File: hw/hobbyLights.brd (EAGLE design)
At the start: 50 x 35 mm, 56 parts, among them U1 MCP73831-2, U2 POWER, U3 BD48K28G, U4 ATMEGA32U4-AU, U5 TPS61222, Y1 RESONATORSMD

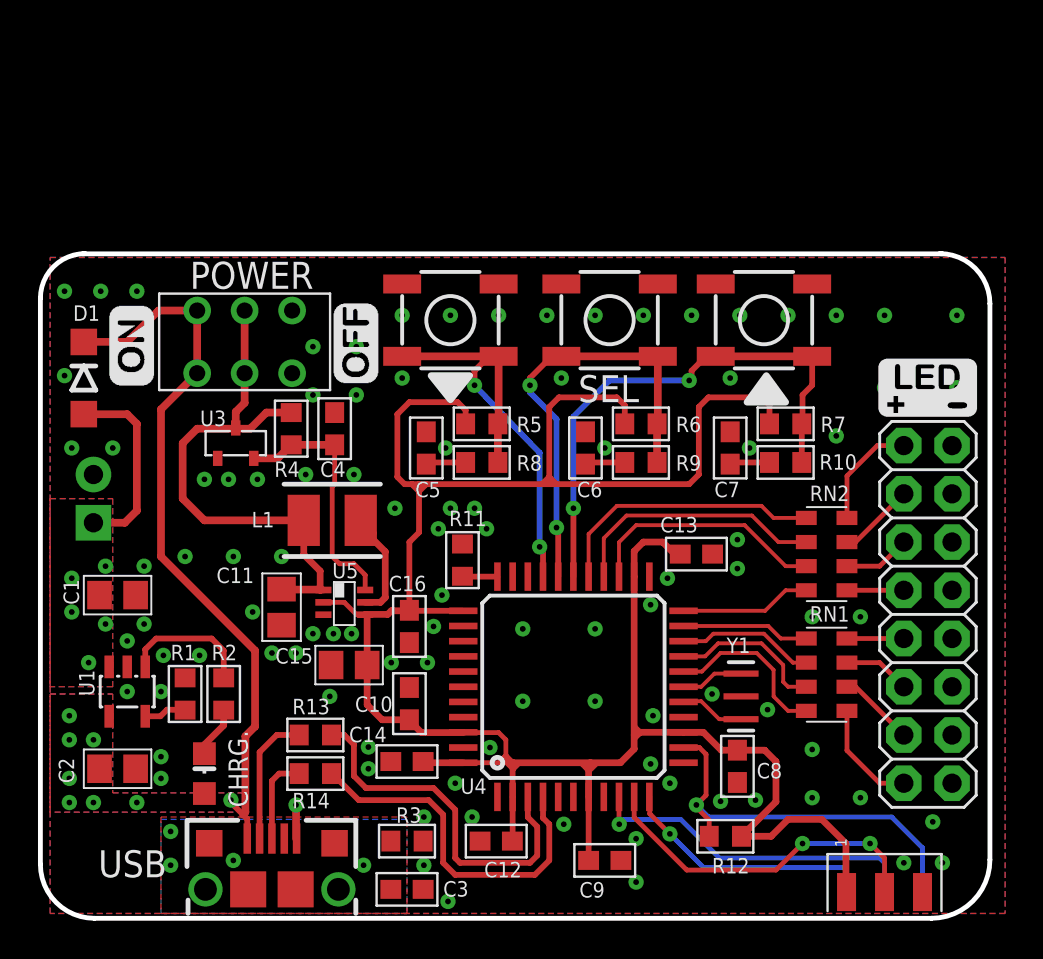
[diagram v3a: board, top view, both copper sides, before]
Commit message: Updated schematic for Rev B.
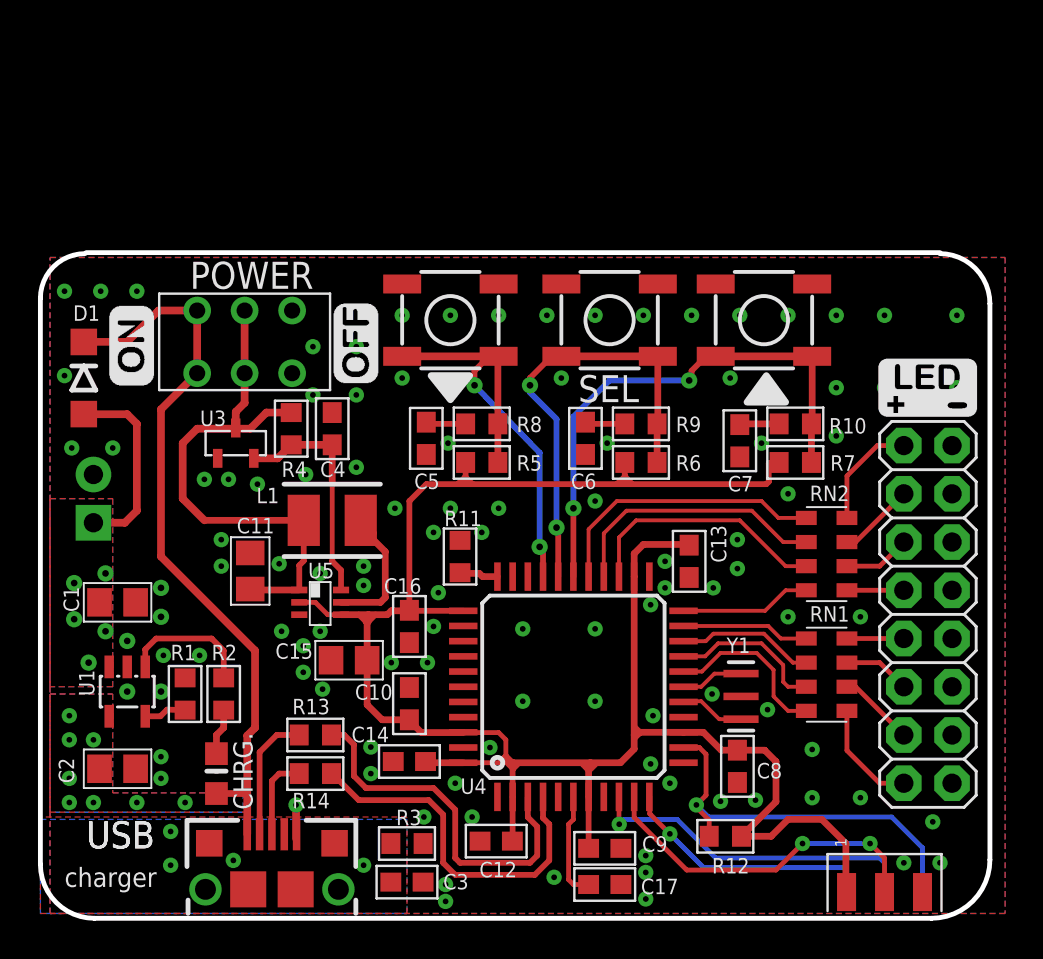
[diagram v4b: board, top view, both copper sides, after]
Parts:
- added C17: 1uF, rcl:C0603
- C5, C6, C7: value 0.1uF -> 0.1nF
- moved C11 2.52 mm to (11.0, 18.3), turned to 90 degrees
- moved R10 2.09 mm to (39.8, 26.0)
- moved R7 2.09 mm to (39.8, 24.0)
- moved R5 2.03 mm to (23.2, 24.0)
- moved R6 2.03 mm to (31.6, 24.0)
- moved R8 2.03 mm to (23.2, 26.0)
- moved R9 2.03 mm to (31.6, 26.0)
- moved U5 1.27 mm to (14.7, 16.6)
- moved CHARGE 0.64 mm to (9.27, 7.62)
- moved C9 0.63 mm to (29.7, 3.68)
- moved C7 0.63 mm to (36.8, 25.1), turned to 270 degrees
- moved C13 0.54 mm to (34.2, 18.8), turned to 270 degrees
- moved C5 0.51 mm to (20.3, 25.3), turned to 270 degrees
- moved C6 0.51 mm to (28.7, 25.3), turned to 270 degrees
- moved C1 0.38 mm to (4.06, 16.6)
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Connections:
- net 3.3V: now also C17.1
- net GND: now also C17.2
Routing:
- net VCC: track 132.7 -> 114.7 mm
- net 3.3V: track 0.00 -> 5.63 mm
- net V_BATT: track 30.9 -> 28.9 mm
- net N$15: track 5.76 -> 7.03 mm
- net PWR_OK: track 13.4 -> 12.3 mm
- net V_USB: track 38.4 -> 38.9 mm
- net GND: track 1.80 -> 2.00 mm, vias 99 -> 106
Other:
- board size 50 x 35 mm -> 50 x 35.1 mm
- board text added: "charger"

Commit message: Updates for production - Rev B
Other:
- board text added: "B"
- board text added: "ICSP"
- board text removed: "A"
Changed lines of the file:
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@@
 <setting verticaltext="up"/>
 </settings>
-<grid distance="0.05" unitdist="inch" unit="mm" style="lines" multiple="1" display="yes" altdistance="5" altunitdist="mil" altunit="mil"/>
+<grid distance="0.05" unitdist="inch" unit="mm" style="lines" multiple="1" display="yes" altdistance="5" altunitdist="mil" altunit="mm"/>
 <layers>
 <layer number="1" name="Top" color="4" fill="1" visible="yes" active="yes"/>
-<layer number="16" name="Bottom" color="1" fill="1" visible="yes" active="yes"/>
+<layer number="16" name="Bottom" color="1" fill="1" visible="no" active="yes"/>
 <layer number="17" name="Pads" color="2" fill="1" visible="yes" active="yes"/>
 <layer number="18" name="Vias" color="2" fill="1" visible="yes" active="yes"/>
@@
 <text x="7.747" y="19.812" size="1.778" layer="22" font="vector" ratio="15" rot="MR0">+</text>
 <text x="33.655" y="15.24" size="1.4224" layer="22" font="vector" ratio="12" rot="MR0">hobby lights</text>
-<text x="33.02" y="11.43" size="1.4224" layer="22" font="vector" ratio="12" rot="MR0">A</text>
+<text x="33.02" y="11.811" size="1.4224" layer="22" font="vector" ratio="12" rot="MR0">B</text>
 <dimension x1="2.35229375" y1="35" x2="5.08" y2="0" x3="-6.35" y3="17.5" textsize="1.4224" textratio="12" layer="47" dtype="vertical"/>
 <dimension x1="0" y1="32.64770625" x2="50.038" y2="29.21" x3="25.019" y3="39.878" textsize="1.4224" textratio="12" layer="47" dtype="horizontal"/>
@@
 <text x="2.413" y="3.683" size="1.4224" layer="21" font="vector" ratio="15">USB</text>
 <text x="1.27" y="1.651" size="1.016" layer="21" font="vector" ratio="15">charger</text>
+<text x="43.434" y="3.81" size="0.8128" layer="21" ratio="12">ICSP</text>
 </plain>
 <attributes>

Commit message: Minor modifications and upgrade to Eagle 7.6.0
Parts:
- RN1, RN2: value (none) -> 470
- S1, S2, S3: value (none) -> microswitch
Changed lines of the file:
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@@
 <?xml version="1.0" encoding="utf-8"?>
 <!DOCTYPE eagle SYSTEM "eagle.dtd">
-<eagle version="7.0.0">
+<eagle version="7.6.0">
 <drawing>
 <settings>
@@
 <layers>
 <layer number="1" name="Top" color="4" fill="1" visible="yes" active="yes"/>
+<layer number="2" name="Route2" color="1" fill="3" visible="no" active="no"/>
+<layer number="15" name="Route15" color="4" fill="6" visible="no" active="no"/>
 <layer number="16" name="Bottom" color="1" fill="1" visible="no" active="yes"/>
 <layer number="17" name="Pads" color="2" fill="1" visible="yes" active="yes"/>
@@
 <attribute name="VALUE" x="16.383" y="9.525" size="0.8128" layer="27" ratio="12" rot="R180"/>
 </element>
-<element name="S1" library="SAVMakerI" package="SPARKFUN_TACTILE_SWITCH_SMD" value="" x="21.59" y="31.496" smashed="yes">
+<element name="S1" library="SAVMakerI" package="SPARKFUN_TACTILE_SWITCH_SMD" value="microswitch" x="21.59" y="31.496" smashed="yes">
 <attribute name="VALUE" x="20.701" y="29.464" size="0.4064" layer="27"/>
 </element>
-<element name="S2" library="SAVMakerI" package="SPARKFUN_TACTILE_SWITCH_SMD" value="" x="29.972" y="31.496" smashed="yes">
+<element name="S2" library="SAVMakerI" package="SPARKFUN_TACTILE_SWITCH_SMD" value="microswitch" x="29.972" y="31.496" smashed="yes">
 <attribute name="VALUE" x="29.083" y="29.464" size="0.4064" layer="27"/>
 </element>
-<element name="S3" library="SAVMakerI" package="SPARKFUN_TACTILE_SWITCH_SMD" value="" x="38.1" y="31.496" smashed="yes">
+<element name="S3" library="SAVMakerI" package="SPARKFUN_TACTILE_SWITCH_SMD" value="microswitch" x="38.1" y="31.496" smashed="yes">
 <attribute name="VALUE" x="37.211" y="29.464" size="0.4064" layer="27"/>
 </element>
@@
 <attribute name="VALUE" x="17.526" y="16.129" size="1.27" layer="27" rot="R180"/>
 </element>
-<element name="RN1" library="resistor-dil" package="EXBS8V" value="" x="41.402" y="12.827" smashed="yes" rot="R270">
+<element name="RN1" library="resistor-dil" package="EXBS8V" value="470" x="41.402" y="12.827" smashed="yes" rot="R270">
 <attribute name="OC_NEWARK" value="unknown" x="41.402" y="12.827" size="1.778" layer="27" rot="R270" display="off"/>
 <attribute name="MPN" value="" x="41.402" y="12.827" size="1.778" layer="27" rot="R270" display="off"/>
@@
 <attribute name="VALUE" x="38.227" y="15.367" size="1.27" layer="27" rot="R270"/>
 </element>
-<element name="RN2" library="resistor-dil" package="EXBS8V" value="" x="41.402" y="19.177" smashed="yes" rot="R270">
+<element name="RN2" library="resistor-dil" package="EXBS8V" value="470" x="41.402" y="19.177" smashed="yes" rot="R270">
 <attribute name="OC_NEWARK" value="unknown" x="41.402" y="19.177" size="1.778" layer="27" rot="R270" display="off"/>
 <attribute name="MPN" value="" x="41.402" y="19.177" size="1.778" layer="27" rot="R270" display="off"/>

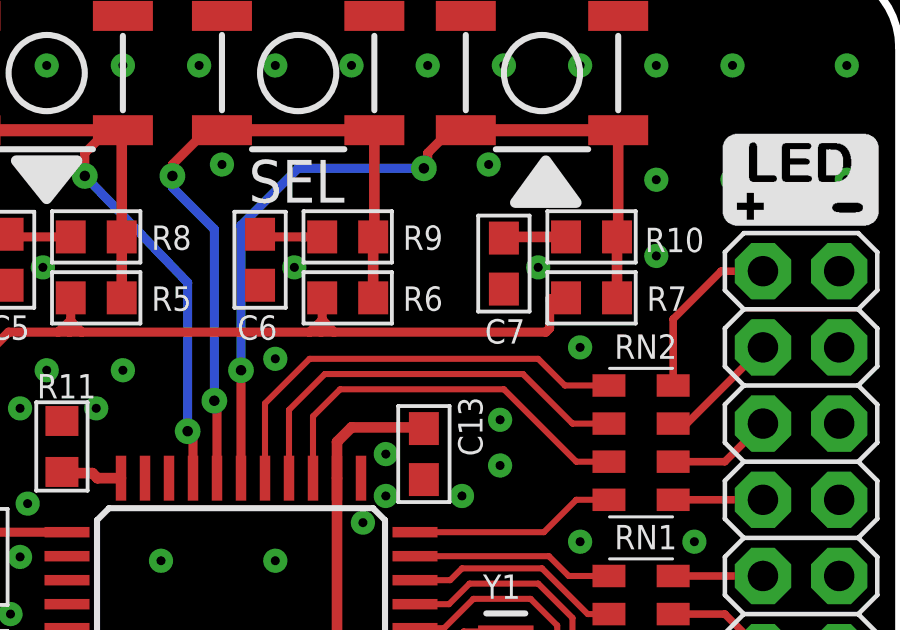
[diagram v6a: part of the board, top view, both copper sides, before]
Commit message: HW: - updated resistor values to increase LED brightness. - updated resistor values to increase charge current. SW: - added new blink program - added new serial line command i.
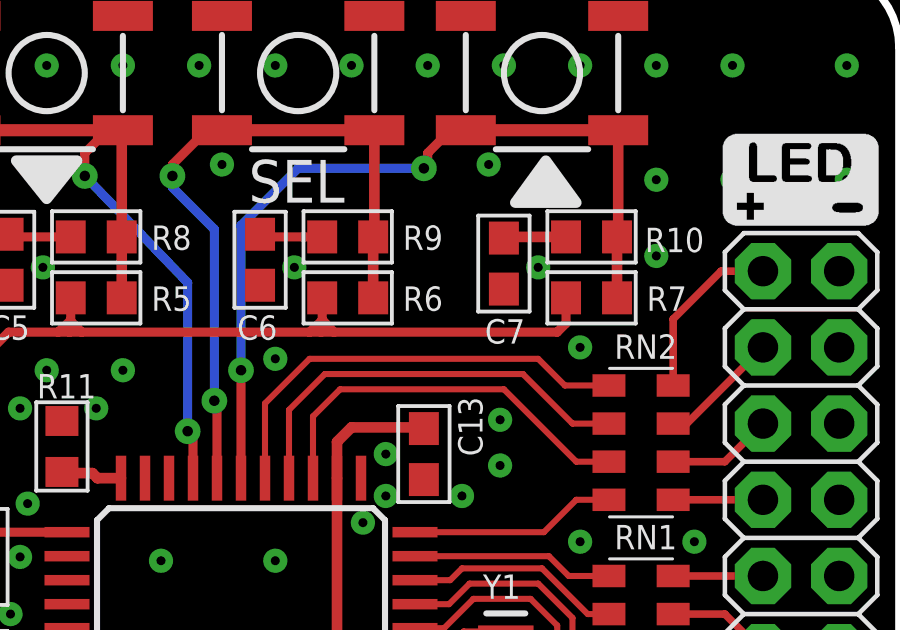
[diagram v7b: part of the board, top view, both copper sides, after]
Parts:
- R1: value 4K7 -> 3.3K
- R2: value 1K -> 470R
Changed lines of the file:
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@@
 <attribute name="VALUE" x="6.477" y="15.113" size="0.8128" layer="27" ratio="12" rot="R180"/>
 </element>
-<element name="R1" library="rcl" package="R0603" value="4K7" x="7.62" y="11.811" smashed="yes" rot="R270">
+<element name="R1" library="rcl" package="R0603" value="3.3K" x="7.62" y="11.811" smashed="yes" rot="R270">
 <attribute name="NAME" x="6.858" y="13.589" size="0.8128" layer="25" ratio="12"/>
 <attribute name="VALUE" x="5.08" y="13.081" size="1.27" layer="27" rot="R270"/>
 </element>
-<element name="R2" library="rcl" package="R0603" value="1K" x="9.652" y="11.811" smashed="yes" rot="R270">
+<element name="R2" library="rcl" package="R0603" value="470R" x="9.652" y="11.811" smashed="yes" rot="R270">
 <attribute name="NAME" x="9.017" y="13.589" size="0.8128" layer="25" ratio="12"/>
 <attribute name="VALUE" x="7.112" y="13.081" size="1.27" layer="27" rot="R270"/>
@@
 <wire x1="17.272" y1="15.621" x2="17.272" y2="15.682" width="0.3556" layer="1"/>
 <wire x1="17.272" y1="15.682" x2="17.206" y2="15.748" width="0.3556" layer="1"/>
-<wire x1="38.354" y1="22.987" x2="38.354" y2="23.964" width="0.3048" layer="1"/>
-<wire x1="38.354" y1="23.964" x2="38.901" y2="24.003" width="0.3048" layer="1"/>
 <wire x1="19.431" y1="21.971" x2="19.431" y2="16.217" width="0.3048" layer="1"/>
-<wire x1="38.354" y1="22.987" x2="38.227" y2="22.86" width="0.3048" layer="1"/>
-<wire x1="38.227" y1="22.86" x2="31.1658" y2="22.86" width="0.3048" layer="1"/>
 <wire x1="30.734" y1="22.86" x2="30.353" y2="22.86" width="0.3048" layer="1"/>
 <wire x1="30.353" y1="22.86" x2="22.7584" y2="22.86" width="0.3048" layer="1"/>
@@
 <wire x1="31.75" y1="19.685" x2="34.124" y2="19.685" width="0.3556" layer="1"/>
 <wire x1="34.124" y1="19.685" x2="34.163" y2="19.646" width="0.3556" layer="1"/>
+<wire x1="31.1658" y1="22.86" x2="38.608" y2="22.86" width="0.3048" layer="1"/>
+<wire x1="38.608" y1="22.86" x2="38.901" y2="23.153" width="0.3048" layer="1"/>
+<wire x1="38.901" y1="24.003" x2="38.901" y2="23.153" width="0.3048" layer="1"/>
 </signal>
 <signal name="RX-I">
